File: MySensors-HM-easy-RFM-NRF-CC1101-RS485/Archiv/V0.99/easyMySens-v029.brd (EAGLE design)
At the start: 65 x 48 mm, 52 parts, among them IC1 ATSHA204A, IC2 REG1117, M1 ARDUINO-PRO-MINI-3.3V#NP, M2 NRF24L01+SMD, X1 1751280, X3 1751280

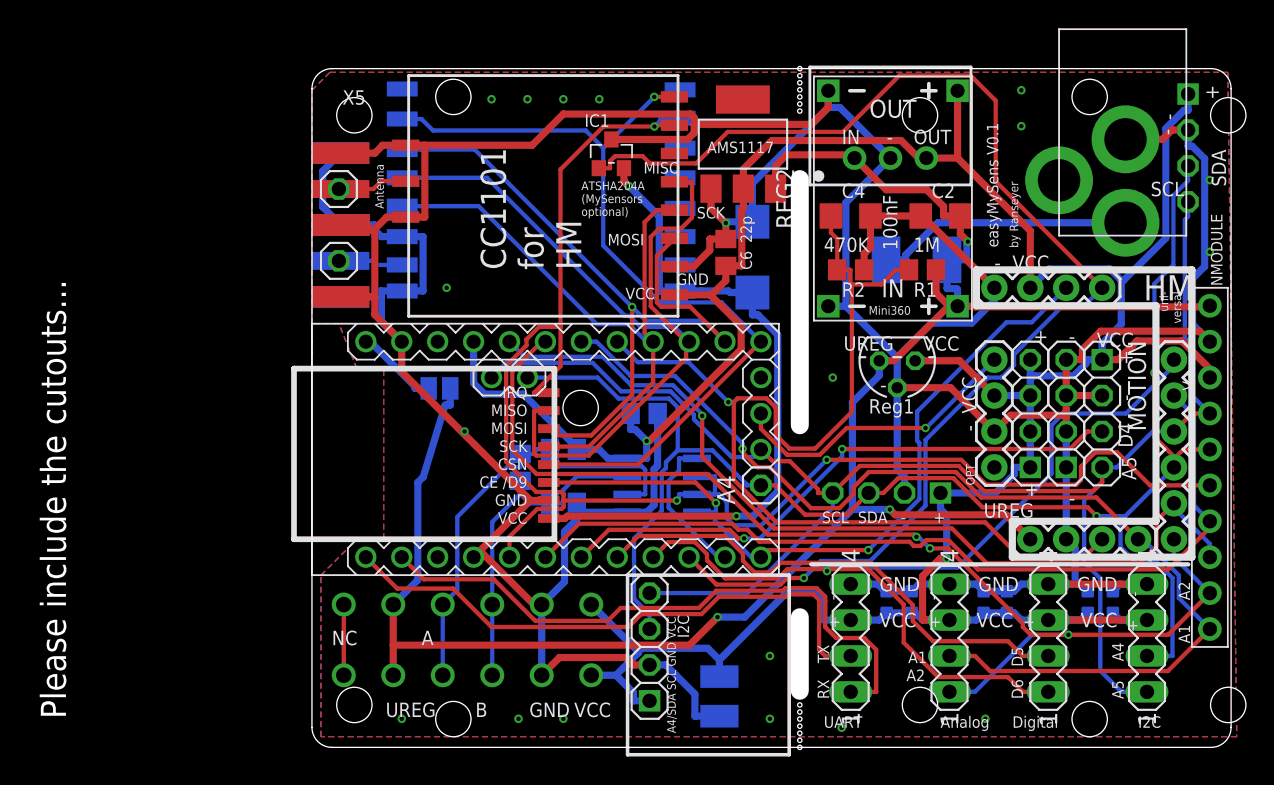
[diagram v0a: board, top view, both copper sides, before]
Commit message: Some new easyBoards
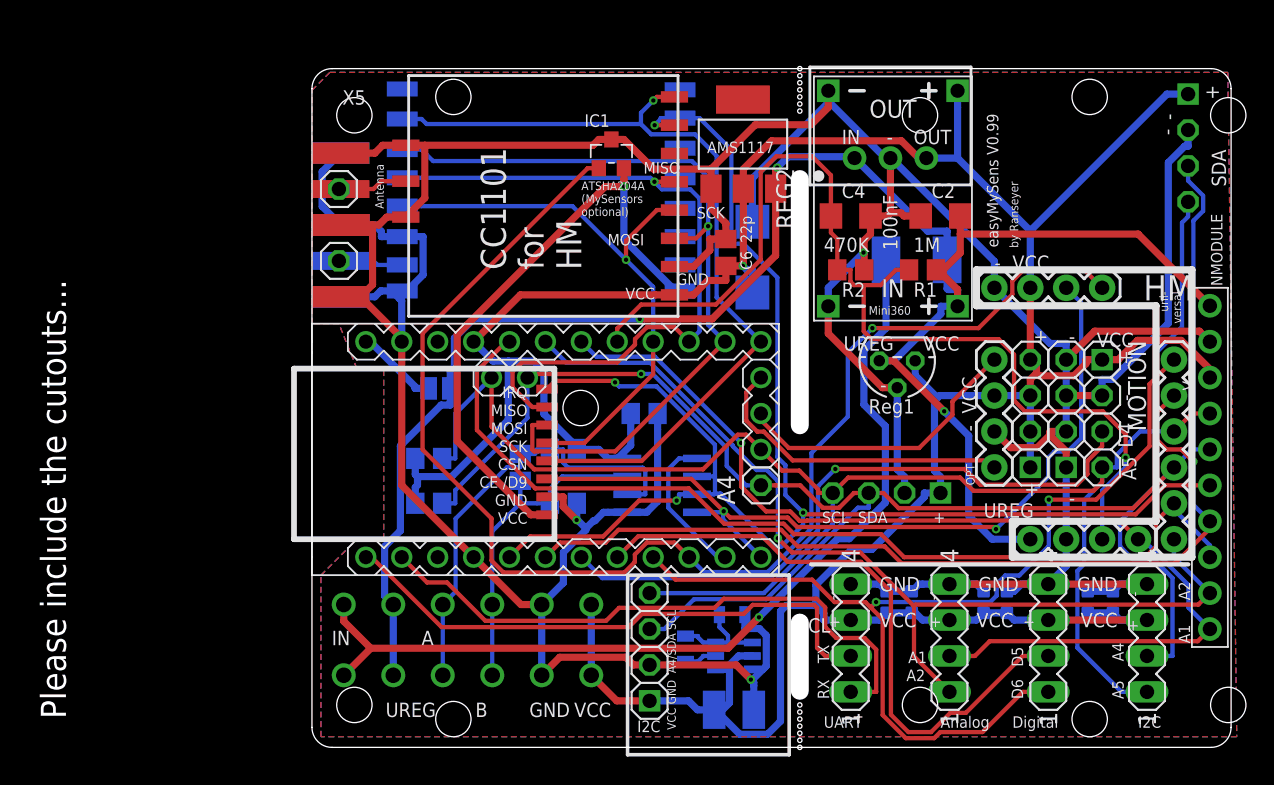
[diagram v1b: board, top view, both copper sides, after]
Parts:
- removed U$3: 2.1MMJACKTHM, adafruit:PJ-102A
- added C5: 10uF, SparkFun-Passives:0805
- added L1: 4,7uH, SparkFun-Passives:0805
- added R3, R7: 10K, rcl:R0805
- added STEPUP: TLV61224, TLV61224:SOT23-6L
- moved C1 1.40 mm to (29.8, 33.7), turned to 180 degrees
- moved M2 0.28 mm to (8.76, 51.6)
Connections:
- removed net FREE: X1.1, X3.1
- new net N$13: L1.2, STEPUP.5
- new net VIN: C5.1, L1.1, STEPUP.1, STEPUP.6
- net 3.3V: no longer C3.+
- net A4: now also R3.2
- net A5: now also R7.2
- net GND: now also C5.2, STEPUP.3; no longer U$3.RING
- net IN: now also X1.1, X3.1; no longer U$3.TIP
- net VCC: now also C3.+, R3.1, R7.1, STEPUP.2, STEPUP.4
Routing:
- net IN: track 18.2 -> 65.7 mm, vias 0 -> 1
- net A7: track 0.00 -> 22.4 mm
- net A4: track 109.3 -> 127.6 mm, vias 2 -> 1
- net VCC: track 221.4 -> 239.1 mm, vias 2 -> 1
- net A5: track 111.8 -> 124.4 mm
- net A2: track 79.8 -> 69.5 mm, vias 3 -> 1
- net D5: track 36.1 -> 44.2 mm
- net MISO: track 59.9 -> 52.0 mm, vias 0 -> 1
- net D9: track 52.6 -> 60.0 mm
- net VIN: track 0.00 -> 7.19 mm
- net ATSHA_D7: track 90.4 -> 96.7 mm
- net 3.3V: track 48.4 -> 42.7 mm, vias 2 -> 1
- net FREE: track 5.00 -> 0.00 mm
- net A3: track 62.9 -> 67.8 mm, vias 1 -> 0
- net D4: track 41.3 -> 45.6 mm, vias 2 -> 1
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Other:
- outline, holes or cut-outs redrawn
- board text added: "VCC GND A4/SDA SCL"
- board text added: "easyMySens V0.99"
- board text removed: "A4/SDA SCL GND VCC"
- board text removed: "NC"
- board text removed: "R4"
- board text removed: "easyMySens V0.1"
